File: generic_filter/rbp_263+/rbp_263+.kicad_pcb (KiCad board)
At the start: 2 copper layers, 36.5 x 52.6 mm, 14 parts, among them J1 Conn_Coaxial, J2 Conn_Coaxial, J3 Conn_Coaxial, J4 Conn_Coaxial, U1 RBP263+/RBP188+

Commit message: updates on Dec 29, 2025
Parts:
- moved J2 4.97 mm to (135.2, 73.8)
- moved U1 4.97 mm to (124.1, 73.8)
- moved H1 4.97 mm to (117.6, 81.4)
- moved H2 4.97 mm to (117.6, 66.4)
- moved H3 4.97 mm to (130.6, 66.4)
- moved H4 4.97 mm to (130.6, 81.4)
- moved J1 4.97 mm to (113.0, 73.8)
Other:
- board size 36.5 x 52.6 mm -> 36.6 x 50.3 mm
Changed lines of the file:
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@@
 	(footprint "minickts_kicad:Mini-Circuits_GP731_LandPatternPL-176"
 		(layer "F.Cu")
-		(at 128.49 71.5)
+		(at 124.11 73.85)
 		(descr "Footprint for Mini-Circuits case GP731 (https://ww2.minicircuits.com/case_style/GP731.pdf) following land pattern PL-176, including GND vias (https://www.minicircuits.com/pcb/98-pl176.pdf)")
 		(tags "mini-circuits PL-176")
@@
 	(footprint "Connector_Coaxial:SMA_Amphenol_132289_EdgeMount"
 		(layer "F.Cu")
-		(at 139.61 71.5)
+		(at 135.23 73.85)
 		(descr "https://www.amphenolrf.com/library/download/link/link_id/595984/parent/132289/")
 		(tags "SMA")
@@
 	(footprint "MountingHole:MountingHole_2.2mm_M2_DIN965_Pad"
 		(layer "F.Cu")
-		(at 135 64.055)
+		(at 130.62 66.405)
 		(descr "Mounting Hole 2.2mm, M2, generated by kicad-footprint-generator mountinghole.py")
 		(tags "mountinghole M2 DIN965")
@@
 	(footprint "MountingHole:MountingHole_2.2mm_M2_DIN965_Pad"
 		(layer "F.Cu")
-		(at 122 79.055)
+		(at 117.62 81.405)
 		(descr "Mounting Hole 2.2mm, M2, generated by kicad-footprint-generator mountinghole.py")
 		(tags "mountinghole M2 DIN965")
@@
 	(footprint "MountingHole:MountingHole_2.2mm_M2_DIN965_Pad"
 		(layer "F.Cu")
-		(at 122 64.055)
+		(at 117.62 66.405)
 		(descr "Mounting Hole 2.2mm, M2, generated by kicad-footprint-generator mountinghole.py")
 		(tags "mountinghole M2 DIN965")
@@
 	(footprint "MountingHole:MountingHole_2.2mm_M2_DIN965_Pad"
 		(layer "F.Cu")
-		(at 135 79.055)
+		(at 130.62 81.405)
 		(descr "Mounting Hole 2.2mm, M2, generated by kicad-footprint-generator mountinghole.py")
 		(tags "mountinghole M2 DIN965")
@@
 	(footprint "Connector_Coaxial:SMA_Amphenol_132289_EdgeMount"
 		(layer "F.Cu")
-		(at 117.3625 71.5 180)
+		(at 112.9825 73.85 180)
 		(descr "https://www.amphenolrf.com/library/download/link/link_id/595984/parent/132289/")
 		(tags "SMA")
@@
 	)
 	(gr_rect
-		(start 114.5 61.555)
-		(end 142.5 81.555)
+		(start 110.12 63.905)
+		(end 138.12 83.905)
 		(stroke
 			(width 0.05)
@@
 	)
 	(gr_text "TOP"
-		(at 137.8 63.92 0)
+		(at 133.42 66.27 0)
 		(layer "F.Cu")
 		(effects
@@
 	)
 	(gr_text "BOT"
-		(at 142.31 63.92 0)
+		(at 137.93 66.27 0)
 		(layer "B.Cu")
 		(effects
@@
 	)
 	(segment
-		(start 117.4175 71.555)
-		(end 117.3625 71.5)
+		(start 113.0375 73.905)
+		(end 112.9825 73.85)
 		(width 0.2)
 		(layer "F.Cu")
@@
 	)
 	(segment
-		(start 117.3625 71.5)
-		(end 120.5 71.5)
+		(start 112.9825 73.85)
+		(end 116.12 73.85)
 		(width 1.5)
 		(layer "F.Cu")
@@
 	)
 	(segment
-		(start 123 71.5)
-		(end 120.5 71.5)
+		(start 118.62 73.85)
+		(end 116.12 73.85)
 		(width 2.5)
 		(layer "F.Cu")
@@
 	)
 	(segment
-		(start 136.41 71.5)
-		(end 134 71.5)
+		(start 132.03 73.85)
+		(end 129.62 73.85)
 		(width 2.5)
 		(layer "F.Cu")
@@
 	)
 	(segment
-		(start 139.61 71.5)
-		(end 136.41 71.5)
+		(start 135.23 73.85)
+		(end 132.03 73.85)
 		(width 1.5)
 		(layer "F.Cu")
@@
 	)
 	(segment
-		(start 136.41 71.5)
-		(end 136.4 71.51)
+		(start 132.03 73.85)
+		(end 132.02 73.86)
 		(width 0.2)
 		(layer "F.Cu")
@@
 	)
 	(segment
-		(start 132.674 71.5)
-		(end 132.619 71.555)
+		(start 128.294 73.85)
+		(end 128.239 73.905)
 		(width 0.2)
 		(layer "F.Cu")
@@
 		(polygon
 			(pts
-				(xy 114.5 74.7) (xy 114.51 81.55) (xy 142.5 81.55) (xy 142.5 74.73)
+				(xy 110.12 77.05) (xy 110.13 83.9) (xy 138.12 83.9) (xy 138.12 77.08)
+			)
+		)
+	)
+	(zone
+		(net 1)
+		(net_name "GND")
+		(layer "F.Cu")
+		(hatch edge 0.5)
+		(priority 3)
+		(connect_pads yes
+			(clearance 0.5)
+		)
+		(min_thickness 0.25)
+		(filled_areas_thickness no)
+		(fill yes
+			(thermal_gap 0.5)
+			(thermal_bridge_width 0.5)
+		)
+		(polygon
+			(pts
+				(xy 110.21 86.41) (xy 110.2 88.89) (xy 129.01 88.97) (xy 129.01 86.4)
 			)
 		)
@@
 		(polygon
 			(pts
-				(xy 142.54 68.21) (xy 114.5 68.2) (xy 114.5 61.55) (xy 142.5 61.55)
+				(xy 138.16 70.56) (xy 110.12 70.55) (xy 110.12 63.9) (xy 138.12 63.9)
+			)
+		)
+	)
+	(zone
+		(net 1)
+		(net_name "GND")
+		(layer "F.Cu")
+		(hatch edge 0.5)
+		(priority 3)
+		(connect_pads yes
+			(clearance 0.5)
+		)
+		(min_thickness 0.25)
+		(filled_areas_thickness no)
+		(fill yes
+			(thermal_gap 0.5)
+			(thermal_bridge_width 0.5)
+		)
+		(polygon
+			(pts
+				(xy 110.168177 95.41) (xy 110.178177 114.18) (xy 146.718177 114.18) (xy 146.708177 110.71) (xy 129.608177 110.700606)
+				(xy 129.608177 103.97) (xy 129.428177 104.18) (xy 146.688177 104.15) (xy 146.708177 86.4) (xy 126.988177 86.4)
+				(xy 126.988177 95.56)
+			)
+		)
+	)
+	(zone
+		(net 0)
+		(net_name "")
+		(layer "F.Mask")
+		(hatch edge 0.5)
+		(priority 3)
+		(connect_pads yes
+			(clearance 0.5)
+		)
+		(min_thickness 0.25)
+		(filled_areas_thickness no)
+		(fill yes
+			(thermal_gap 0.5)
+			(thermal_bridge_width 0.5)
+		)
+		(polygon
+			(pts
+				(xy 110.22 86.41) (xy 110.2 114.16) (xy 146.74 114.16) (xy 146.74 86.4)
 			)
 		)
@@
 		(polygon
 			(pts
-				(xy 114.5 61.55) (xy 114.51 81.55) (xy 142.5 81.55) (xy 142.5 61.55)
+				(xy 110.12 63.9) (xy 110.13 83.9) (xy 138.12 83.9) (xy 138.12 63.9)
+			)
+		)
+	)
+	(zone
+		(net 1)
+		(net_name "GND")
+		(layer "B.Cu")
+		(hatch edge 0.5)
+		(priority 5)
+		(connect_pads yes
+			(clearance 0.5)
+		)
+		(min_thickness 0.25)
+		(filled_areas_thickness no)
+		(fill yes
+			(thermal_gap 0.5)
+			(thermal_bridge_width 0.5)
+		)
+		(polygon
+			(pts
+				(xy 146.75 86.42) (xy 146.74 114.17) (xy 110.2 114.17) (xy 110.2 86.41)
 			)
 		)
@@
 		(polygon
 			(pts
-				(xy 114.51 61.56) (xy 114.5 81.56) (xy 142.51 81.56) (xy 142.5 61.55)
+				(xy 110.13 63.91) (xy 110.12 83.91) (xy 138.13 83.91) (xy 138.12 63.9)
 			)
 		)
@@
 		(polygon
 			(pts
-				(xy 114.51 61.56) (xy 114.5 81.56) (xy 142.51 81.56) (xy 142.5 61.55)
+				(xy 110.13 63.91) (xy 110.12 83.91) (xy 138.13 83.91) (xy 138.12 63.9)
+			)
+		)
+	)
+	(zone
+		(net 0)
+		(net_name "")
+		(layer "B.Mask")
+		(hatch edge 0.5)
+		(priority 3)
+		(connect_pads yes
+			(clearance 0.5)
+		)
+		(min_thickness 0.25)
+		(filled_areas_thickness no)
+		(fill yes
+			(thermal_gap 0.5)
+			(thermal_bridge_width 0.5)
+		)
+		(polygon
+			(pts
+				(xy 110.2 86.41) (xy 110.2 114.17) (xy 146.75 114.17) (xy 146.75 86.42)
 			)
 		)

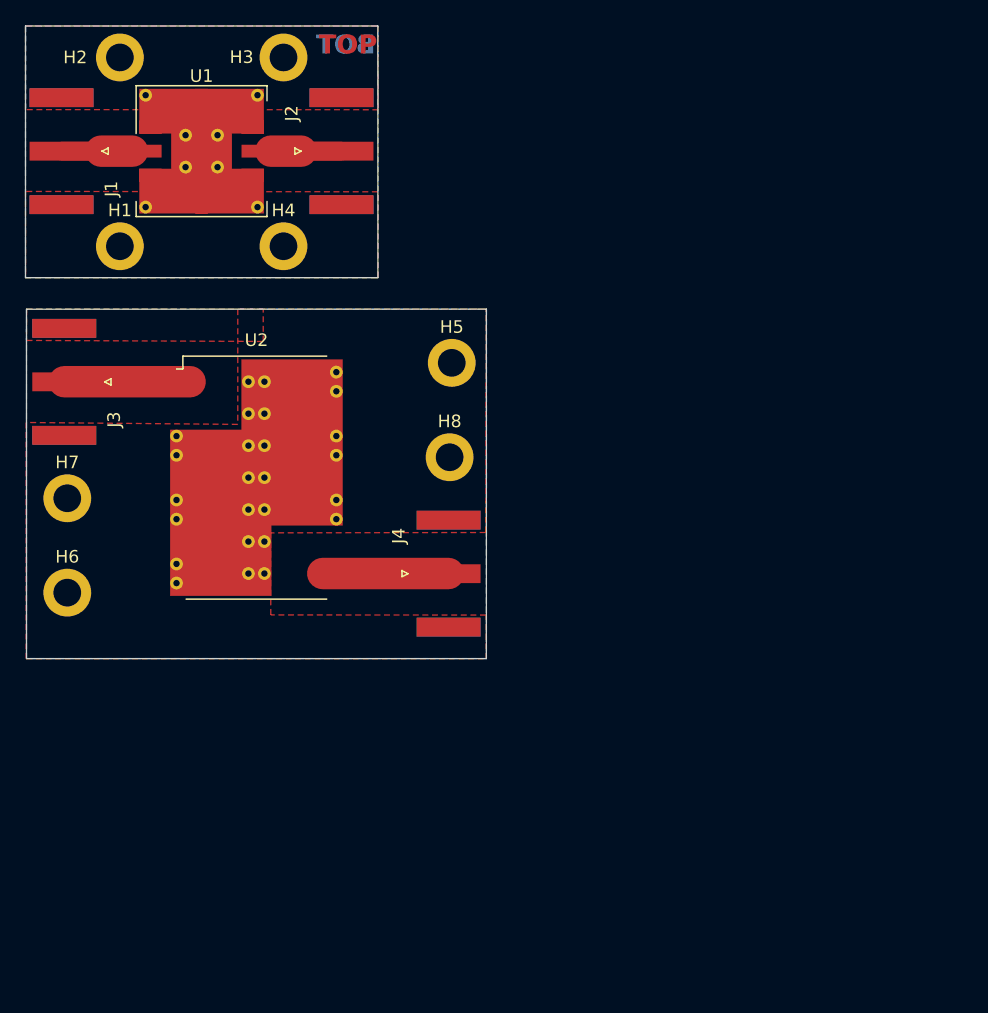
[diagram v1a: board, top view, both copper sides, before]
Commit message: included all amp ckts
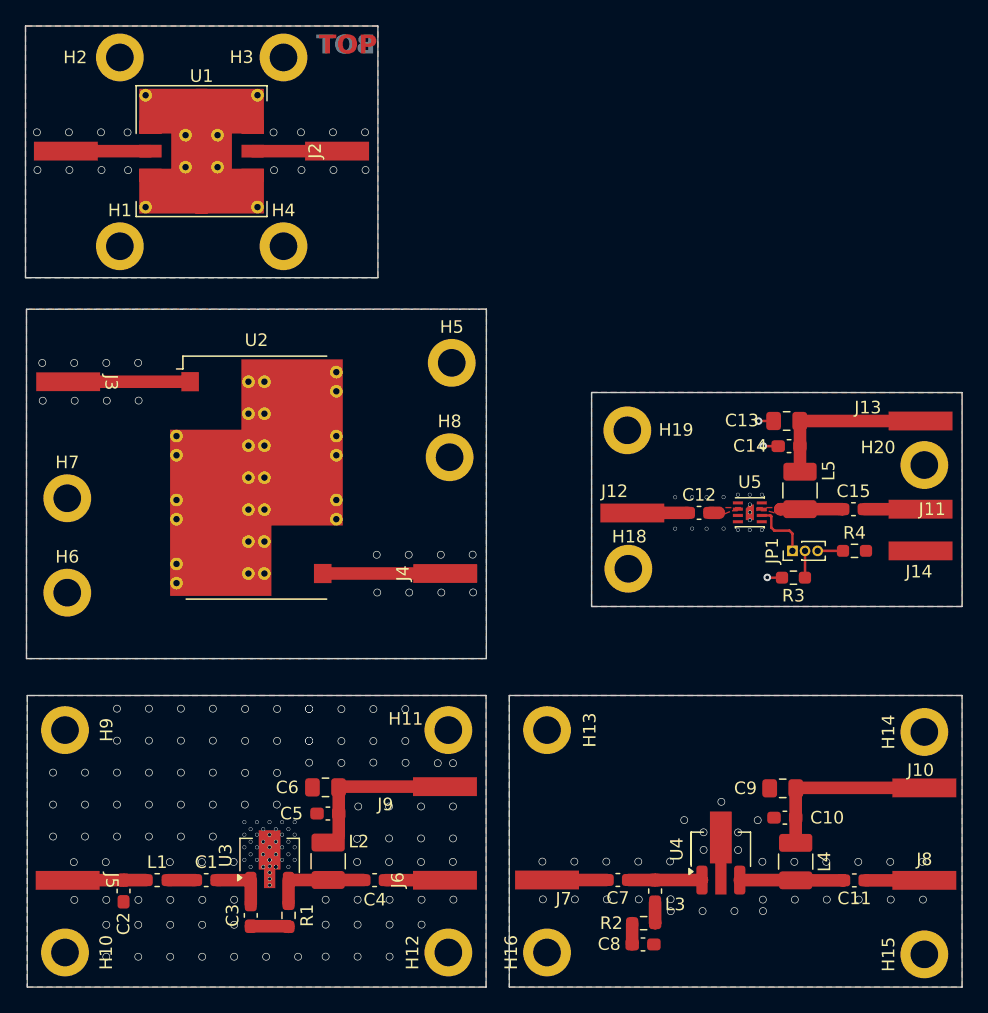
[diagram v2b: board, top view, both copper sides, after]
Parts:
- added C1: C_Small, Capacitor_SMD:C_0603_1608Metric_Pad1.08x0.95mm_HandSolder, F.Cu at (124.5, 131.8)
- added C10: C_Small, Capacitor_SMD:C_0603_1608Metric_Pad1.08x0.95mm_HandSolder, F.Cu at (170.5, 126.8)
- added C11: C_Small, Capacitor_SMD:C_0603_1608Metric_Pad1.08x0.95mm_HandSolder, F.Cu at (176.0, 131.8)
- added C12: C_Small, Capacitor_SMD:C_0603_1608Metric_Pad1.08x0.95mm_HandSolder, F.Cu at (163.6, 102.6)
- added C13: C_Small, Capacitor_SMD:C_0805_2012Metric_Pad1.18x1.45mm_HandSolder, F.Cu at (170.6, 95.3)
- added C14: C_Small, Capacitor_SMD:C_0603_1608Metric_Pad1.08x0.95mm_HandSolder, F.Cu at (170.8, 97.3)
- added C15: C_Small, Capacitor_SMD:C_0603_1608Metric_Pad1.08x0.95mm_HandSolder, F.Cu at (175.9, 102.3)
- added C2: C_Small, Capacitor_SMD:C_0603_1608Metric_Pad1.08x0.95mm_HandSolder, F.Cu at (117.9, 132.6)
- added C3: C_Small, Capacitor_SMD:C_0603_1608Metric_Pad1.08x0.95mm_HandSolder, F.Cu at (128.0, 134.6)
- added C4: C_Small, Capacitor_SMD:C_0603_1608Metric_Pad1.08x0.95mm_HandSolder, F.Cu at (137.9, 131.8)
- added C5: C_Small, Capacitor_SMD:C_0603_1608Metric_Pad1.08x0.95mm_HandSolder, F.Cu at (134.1, 126.5)
- added C6: C_Small, Capacitor_SMD:C_0805_2012Metric_Pad1.18x1.45mm_HandSolder, F.Cu at (134.0, 124.4)
- added C7: C_Small, Capacitor_SMD:C_0603_1608Metric_Pad1.08x0.95mm_HandSolder, F.Cu at (157.2, 131.8)
- added C8: C_Small, Capacitor_SMD:C_0603_1608Metric_Pad1.08x0.95mm_HandSolder, F.Cu at (159.2, 136.9)
- added C9: C_Small, Capacitor_SMD:C_0805_2012Metric_Pad1.18x1.45mm_HandSolder, F.Cu at (170.3, 124.5)
- added H10: MountingHole_Pad, MountingHole:MountingHole_2.2mm_M2_DIN965_Pad, F.Cu at (113.3, 137.5)
- added H11: MountingHole_Pad, MountingHole:MountingHole_2.2mm_M2_DIN965_Pad, F.Cu at (143.7, 119.8)
- added H12: MountingHole_Pad, MountingHole:MountingHole_2.2mm_M2_DIN965_Pad, F.Cu at (143.7, 137.5)
- added H13: MountingHole_Pad, MountingHole:MountingHole_2.2mm_M2_DIN965_Pad, F.Cu at (151.6, 119.8)
- added H14: MountingHole_Pad, MountingHole:MountingHole_2.2mm_M2_DIN965_Pad, F.Cu at (181.5, 120.0)
- added H15: MountingHole_Pad, MountingHole:MountingHole_2.2mm_M2_DIN965_Pad, F.Cu at (181.5, 137.7)
- added H16: MountingHole_Pad, MountingHole:MountingHole_2.2mm_M2_DIN965_Pad, F.Cu at (151.6, 137.5)
- added H18: MountingHole_Pad, MountingHole:MountingHole_2.2mm_M2_DIN965_Pad, F.Cu at (158.0, 107.0)
- added H19: MountingHole_Pad, MountingHole:MountingHole_2.2mm_M2_DIN965_Pad, F.Cu at (157.9, 96.0)
- added H20: MountingHole_Pad, MountingHole:MountingHole_2.2mm_M2_DIN965_Pad, F.Cu at (181.5, 98.8)
- added H9: MountingHole_Pad, MountingHole:MountingHole_2.2mm_M2_DIN965_Pad, F.Cu at (113.3, 119.8)
- added J10: +5V, PanelMountRF_DC:RF_SMA_Edge_PanelMount, F.Cu at (181.2, 124.4)
- added J11: RF_OUT, PanelMountRF_DC:RF_SMA_Edge_PanelMount, F.Cu at (181.2, 102.3)
- added J12: RF_OUT, PanelMountRF_DC:RF_SMA_Edge_PanelMount, F.Cu at (158.3, 102.6)
- added J13: +5V, PanelMountRF_DC:RF_SMA_Edge_PanelMount, F.Cu at (180.5, 95.3)
- added J14: VSHUT, PanelMountRF_DC:RF_SMA_Edge_PanelMount, F.Cu at (181.2, 105.6)
- added J5: RF_IN, PanelMountRF_DC:RF_SMA_Edge_PanelMount, F.Cu at (113.5, 131.8)
- added J6: RF_OUT, PanelMountRF_DC:RF_SMA_Edge_PanelMount, F.Cu at (143.4, 131.8)
- added J7: RF_IN, PanelMountRF_DC:RF_SMA_Edge_PanelMount, F.Cu at (152.9, 131.8)
- added J8: RF_IN, PanelMountRF_DC:RF_SMA_Edge_PanelMount, F.Cu at (181.5, 131.8)
- added J9: +5V, PanelMountRF_DC:RF_SMA_Edge_PanelMount, F.Cu at (138.7, 124.3)
- added JP1: Jumper_3_Bridged12, Connector_PinHeader_1.00mm:PinHeader_1x03_P1.00mm_Vertical, F.Cu at (171.1, 105.6)
- added L1: L_Small, Inductor_SMD:L_0603_1608Metric_Pad1.05x0.95mm_HandSolder, F.Cu at (120.6, 131.8)
- added L2: L_Small, Inductor_SMD:L_1210_3225Metric_Pad1.42x2.65mm_HandSolder, F.Cu at (134.2, 130.3)
- added L3: L_Small, Inductor_SMD:L_0603_1608Metric_Pad1.05x0.95mm_HandSolder, F.Cu at (160.1, 132.6)
- added L4: L_Small, Inductor_SMD:L_1210_3225Metric_Pad1.42x2.65mm_HandSolder, F.Cu at (171.3, 130.3)
- added L5: L_Small, Inductor_SMD:L_1210_3225Metric_Pad1.42x2.65mm_HandSolder, F.Cu at (171.7, 100.8)
- added R1: R_Small, Resistor_SMD:R_0603_1608Metric_Pad0.98x0.95mm_HandSolder, F.Cu at (131.0, 134.6)
- added R2: R_Small, Resistor_SMD:R_0603_1608Metric_Pad0.98x0.95mm_HandSolder, F.Cu at (159.2, 135.2)
- added R3: R_Small, Resistor_SMD:R_0603_1608Metric_Pad0.98x0.95mm_HandSolder, F.Cu at (171.1, 107.7)
- added R4: R_Small, Resistor_SMD:R_0603_1608Metric_Pad0.98x0.95mm_HandSolder, F.Cu at (176.0, 105.6)
- added U3: PHA-13LN, Package_TO_SOT_SMD:SOT-89-3, F.Cu at (129.5, 129.8)
- added U4: ~, Package_TO_SOT_SMD:SOT-89-3_Handsoldering, F.Cu at (165.4, 129.3)
- added U5: ~, minickts_kicad:QFN-8_EP_2x2_Pitch0.5mm, F.Cu at (167.7, 102.5)
- J1, J3: value Conn_Coaxial -> RF_IN; footprint Connector_Coaxial:SMA_Amphenol_132289_EdgeMount -> PanelMountRF_DC:RF_SMA_Edge_PanelMount
- J2, J4: value Conn_Coaxial -> RF_OUT; footprint Connector_Coaxial:SMA_Amphenol_132289_EdgeMount -> PanelMountRF_DC:RF_SMA_Edge_PanelMount
- moved J2 0.35 mm to (134.9, 73.8), turned to 90 degrees
- moved J1 0.35 mm to (113.3, 73.8), turned to -90 degrees
- moved J3 0.31 mm to (113.5, 92.2), turned to -90 degrees
- moved J4 0.09 mm to (143.7, 107.4), turned to 90 degrees
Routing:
- net Net-(J10-Pin_1): track 0.00 -> 14.7 mm
- net Net-(J13-Pin_1): track 0.00 -> 13.6 mm
- net Net-(J9-Pin_1): track 0.00 -> 12.7 mm
- net Net-(U4-RFOUT): track 0.00 -> 8.25 mm
- net Net-(C4-Pad1): track 0.00 -> 7.81 mm
- net Net-(J5-Pin_1): track 0.00 -> 6.57 mm
- net Net-(U4-RFIN): track 0.00 -> 5.82 mm
- net Net-(J6-Pin_1): track 0.00 -> 5.06 mm
- net Net-(U5-RF-OUT+Vdd): track 0.00 -> 4.97 mm
- net Net-(JP1-A): track 0.00 -> 4.93 mm
- net Net-(J7-Pin_1): track 0.00 -> 4.76 mm
- net Net-(J8-Pin_1): track 0.00 -> 4.70 mm
- net Net-(C1-Pad2): track 0.00 -> 4.61 mm
- net Net-(J11-Pin_1): track 0.00 -> 4.47 mm
- net Net-(J12-Pin_1): track 0.00 -> 4.44 mm
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- added copper zone on F.Cu, net Net-(U5-RF-IN)
- added copper zone on F.Cu, net Net-(U5-RF-OUT+Vdd)
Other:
- board size 36.6 x 50.3 mm -> 74.4 x 76.4 mm
